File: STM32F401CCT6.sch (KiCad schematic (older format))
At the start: 37 parts, among them J1 USB_OTG, J2 Conn_02x03_Odd_Even, J3 Conn_01x20_des, J4 Conn_01x05_desc, J5 Conn_01x20, SW1 SW_Push, U1 MIC5219-3.3, U2 STM32F401CCT6, U3 USBLC6-2SC6, Y1 32.786K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

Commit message: routing
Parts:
- J1: footprint Connectors_USB:USB_Micro-B_Molex_47346-0001 -> Connectors_USB:USB_Micro-B_Molex-105017-0001
- J2: footprint Pin_Headers:Pin_Header_Straight_2x03_Pitch2.54mm_SMD -> Pin_Headers:Pin_Header_Straight_2x03_Pitch2.54mm
- Y2: footprint Crystals:Crystal_HC49-U_Vertical -> Crystals:Crystal_HC49-4H_Vertical
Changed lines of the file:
@@
 F 0 "J2" H 2750 1400 50  0000 C CNN
 F 1 "Conn_02x03_Odd_Even" H 2750 1000 50  0000 C CNN
-F 2 "Pin_Headers:Pin_Header_Straight_2x03_Pitch2.54mm_SMD" H 2700 1200 50  0001 C CNN
+F 2 "Pin_Headers:Pin_Header_Straight_2x03_Pitch2.54mm" H 2700 1200 50  0001 C CNN
 F 3 "" H 2700 1200 50  0001 C CNN
 	1    2700 1200
@@
 F 0 "J1" H 700 6750 50  0000 L CNN
 F 1 "USB_OTG" H 700 6650 50  0000 L CNN
-F 2 "Connectors_USB:USB_Micro-B_Molex_47346-0001" H 1050 6250 50  0001 C CNN
+F 2 "Connectors_USB:USB_Micro-B_Molex-105017-0001" H 1050 6250 50  0001 C CNN
 F 3 "" H 1050 6250 50  0001 C CNN
 	1    900  6300
@@
 F 0 "Y2" V 4750 6900 50  0000 C CNN
 F 1 "8MHz" V 4650 6950 50  0000 C CNN
-F 2 "Crystals:Crystal_HC49-U_Vertical" H 4750 6750 50  0001 C CNN
+F 2 "Crystals:Crystal_HC49-4H_Vertical" H 4750 6750 50  0001 C CNN
 F 3 "" H 4750 6750 50  0001 C CNN
 	1    4750 6750

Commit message: Added copper pour
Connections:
- net VCC3v3 is gone; now on net VCC: J3.18 (Pin_18), J5.1 (Pin_1), U2.24 (VDD_2), U2.36 (VDD_2), U2.48 (VDD_3), U2.9 (VDDA/VREF+)
- net +5V: now also C14.1, J4.5 (Pin_5)
- net GND: no longer C14.1, J4.4 (Pin_4)
- net RESET: now also J4.4 (Pin_4); no longer J4.5 (Pin_5)
- net D-: now reaches J1.2 (D-), R3.2
- net D+: now reaches J1.3 (D+), R4.2
- net ID: now reaches J1.4 (ID), R9.2

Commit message: rerouting (left reset)
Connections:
- net +5V: no longer C14.1, J4.5 (Pin_5)
- net GND: no longer R6.1
- net PC13: now also R6.1
- net VCC: now also C14.1, J4.5 (Pin_5)
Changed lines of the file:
@@
 $EndComp
 Text Label 6300 1550 2    60   ~ 0
-GND
+PC13
 $Comp
 L Conn_02x03_Odd_Even J2
@@
 $EndComp
 Text Label 8500 1450 2    60   ~ 0
-STM_LINK
+VCC
 $Comp
 L Conn_01x20_des J3

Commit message: Finish routing
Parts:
- D1, D2: footprint LEDs:LED_0603_HandSoldering -> LEDs:LED_0805_HandSoldering
- U2: footprint UFQFPN48:UFQFPN48 -> QFPN48:UFQFPN48
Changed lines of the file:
@@
 F 0 "U2" H 7250 4450 60  0000 C CNN
 F 1 "STM32F401CCT6" H 7300 4350 50  0000 C CNN
-F 2 "UFQFPN48:UFQFPN48" H 5700 3850 60  0001 C CNN
+F 2 "QFPN48:UFQFPN48" H 5700 3850 60  0001 C CNN
 F 3 "" H 5700 3850 60  0001 C CNN
 	1    5700 3850
@@
 F 0 "D1" H 5250 1150 50  0000 C CNN
 F 1 "LED_ALT" H 5250 950 50  0000 C CNN
-F 2 "LEDs:LED_0603_HandSoldering" H 5250 1050 50  0001 C CNN
+F 2 "LEDs:LED_0805_HandSoldering" H 5250 1050 50  0001 C CNN
 F 3 "" H 5250 1050 50  0001 C CNN
 	1    5250 1050
@@
 F 0 "D2" H 5250 1650 50  0000 C CNN
 F 1 "LED_ALT" H 5250 1450 50  0000 C CNN
-F 2 "LEDs:LED_0603_HandSoldering" H 5250 1550 50  0001 C CNN
+F 2 "LEDs:LED_0805_HandSoldering" H 5250 1550 50  0001 C CNN
 F 3 "" H 5250 1550 50  0001 C CNN
 	1    5250 1550

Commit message: Moved the pin connector to bottom layer
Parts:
- C1, C10, C11, C12, C13, C14, C2, C3, C4, C5, C6, C7, C8, C9: footprint Capacitors_SMD:C_0603_HandSoldering -> Capacitors_SMD:C_0603
- D1, D2: footprint LEDs:LED_0805_HandSoldering -> LEDs:LED_0805
- R1, R10, R2, R3, R4, R5, R6, R7, R8, R9: footprint Resistors_SMD:R_0603_HandSoldering -> Resistors_SMD:R_0603
- U1: footprint TO_SOT_Packages_SMD:SOT-23-5_HandSoldering -> TO_SOT_Packages_SMD:SOT-23-5
- U3: footprint TO_SOT_Packages_SMD:SOT-23-6_Handsoldering -> TO_SOT_Packages_SMD:SOT-23-6
- Y1: footprint Crystals:Crystal_SMD_SeikoEpson_MC306-4pin_8.0x3.2mm_HandSoldering -> Crystals:Crystal_SMD_SeikoEpson_MC306-4pin_8.0x3.2mm
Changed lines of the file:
@@
 F 0 "R5" V 6030 1050 50  0000 C CNN
 F 1 "510R,0603" V 5850 1050 50  0000 C CNN
-F 2 "Resistors_SMD:R_0603_HandSoldering" V 5880 1050 50  0001 C CNN
+F 2 "Resistors_SMD:R_0603" V 5880 1050 50  0001 C CNN
 F 3 "" H 5950 1050 50  0001 C CNN
 	1    5950 1050
@@
 F 0 "R6" V 6030 1550 50  0000 C CNN
 F 1 "510R,603" V 5850 1550 50  0000 C CNN
-F 2 "Resistors_SMD:R_0603_HandSoldering" V 5880 1550 50  0001 C CNN
+F 2 "Resistors_SMD:R_0603" V 5880 1550 50  0001 C CNN
 F 3 "" H 5950 1550 50  0001 C CNN
 	1    5950 1550
@@
 F 0 "R8" V 3330 1200 50  0000 C CNN
 F 1 "100K,0603" V 3100 1200 50  0000 C CNN
-F 2 "Resistors_SMD:R_0603_HandSoldering" V 3180 1200 50  0001 C CNN
+F 2 "Resistors_SMD:R_0603" V 3180 1200 50  0001 C CNN
 F 3 "" H 3250 1200 50  0001 C CNN
 	1    3250 1200
@@
 F 0 "R7" V 2230 1200 50  0000 C CNN
 F 1 "100K,0603" V 2000 1200 50  0000 C CNN
-F 2 "Resistors_SMD:R_0603_HandSoldering" V 2080 1200 50  0001 C CNN
+F 2 "Resistors_SMD:R_0603" V 2080 1200 50  0001 C CNN
 F 3 "" H 2150 1200 50  0001 C CNN
 	1    2150 1200
@@
 F 0 "R1" V 1130 1200 50  0000 C CNN
 F 1 "10K" V 1050 1200 50  0000 C CNN
-F 2 "Resistors_SMD:R_0603_HandSoldering" V 980 1200 50  0001 C CNN
+F 2 "Resistors_SMD:R_0603" V 980 1200 50  0001 C CNN
 F 3 "" H 1050 1200 50  0001 C CNN
 	1    1050 1200
@@
 F 0 "C3" H 1075 1700 50  0000 L CNN
 F 1 "105,0603" H 1075 1500 50  0000 L CNN
-F 2 "Capacitors_SMD:C_0603_HandSoldering" H 1088 1450 50  0001 C CNN
+F 2 "Capacitors_SMD:C_0603" H 1088 1450 50  0001 C CNN
 F 3 "" H 1050 1600 50  0001 C CNN
 	1    1050 1600
@@
 F 0 "R3" V 1800 6300 50  0000 C CNN
 F 1 "20R,0603" V 1700 6350 50  0000 C CNN
-F 2 "Resistors_SMD:R_0603_HandSoldering" V 1730 6300 50  0001 C CNN
+F 2 "Resistors_SMD:R_0603" V 1730 6300 50  0001 C CNN
 F 3 "" H 1800 6300 50  0001 C CNN
 	1    1800 6300
@@
 F 0 "R4" V 1800 6400 50  0000 C CNN
 F 1 "20R,0603" V 1900 6450 50  0000 C CNN
-F 2 "Resistors_SMD:R_0603_HandSoldering" V 1730 6400 50  0001 C CNN
+F 2 "Resistors_SMD:R_0603" V 1730 6400 50  0001 C CNN
 F 3 "" H 1800 6400 50  0001 C CNN
 	1    1800 6400
@@
 F 0 "R10" V 2150 6650 50  0000 C CNN
 F 1 "4.7K" V 2250 6650 50  0000 C CNN
-F 2 "Resistors_SMD:R_0603_HandSoldering" V 2080 6650 50  0001 C CNN
+F 2 "Resistors_SMD:R_0603" V 2080 6650 50  0001 C CNN
 F 3 "" H 2150 6650 50  0001 C CNN
 	1    2150 6650
@@
 F 0 "C6" V 4100 5550 50  0000 L CNN
 F 1 "20p,0603" V 4000 5550 50  0000 L CNN
-F 2 "Capacitors_SMD:C_0603_HandSoldering" H 4188 5550 50  0001 C CNN
+F 2 "Capacitors_SMD:C_0603" H 4188 5550 50  0001 C CNN
 F 3 "" H 4150 5700 50  0001 C CNN
 	1    4150 5700
@@
 F 0 "C7" V 4100 6050 50  0000 L CNN
 F 1 "20p,0603" V 4000 6000 50  0000 L CNN
-F 2 "Capacitors_SMD:C_0603_HandSoldering" H 4188 6050 50  0001 C CNN
+F 2 "Capacitors_SMD:C_0603" H 4188 6050 50  0001 C CNN
 F 3 "" H 4150 6200 50  0001 C CNN
 	1    4150 6200
@@
 F 0 "C10" H 4575 5200 50  0000 L CNN
 F 1 "104,0603" H 4575 5000 50  0000 L CNN
-F 2 "Capacitors_SMD:C_0603_HandSoldering" H 4588 4950 50  0001 C CNN
+F 2 "Capacitors_SMD:C_0603" H 4588 4950 50  0001 C CNN
 F 3 "" H 4550 5100 50  0001 C CNN
 	1    4550 5100
@@
 F 0 "C11" H 4975 5200 50  0000 L CNN
 F 1 "104,0603" H 4975 5000 50  0000 L CNN
-F 2 "Capacitors_SMD:C_0603_HandSoldering" H 4988 4950 50  0001 C CNN
+F 2 "Capacitors_SMD:C_0603" H 4988 4950 50  0001 C CNN
 F 3 "" H 4950 5100 50  0001 C CNN
 	1    4950 5100
@@
 F 0 "C14" H 8725 1300 50  0000 L CNN
 F 1 "104,0603" H 8725 1100 50  0000 L CNN
-F 2 "Capacitors_SMD:C_0603_HandSoldering" H 8738 1050 50  0001 C CNN
+F 2 "Capacitors_SMD:C_0603" H 8738 1050 50  0001 C CNN
 F 3 "" H 8700 1200 50  0001 C CNN
 	1    8700 1200
@@
 F 0 "Y1" V 4450 6150 50  0000 C CNN
 F 1 "32.786K" V 4350 6200 50  0000 C CNN
-F 2 "Crystals:Crystal_SMD_SeikoEpson_MC306-4pin_8.0x3.2mm_HandSoldering" H 4450 5950 50  0001 C CNN
+F 2 "Crystals:Crystal_SMD_SeikoEpson_MC306-4pin_8.0x3.2mm" H 4450 5950 50  0001 C CNN
 F 3 "" H 4450 5950 50  0001 C CNN
 	1    4450 5950
@@
 F 0 "C8" V 4300 6500 50  0000 L CNN
 F 1 "20p,0603" V 4550 6300 50  0000 L CNN
-F 2 "Capacitors_SMD:C_0603_HandSoldering" H 4438 6300 50  0001 C CNN
+F 2 "Capacitors_SMD:C_0603" H 4438 6300 50  0001 C CNN
 F 3 "" H 4400 6450 50  0001 C CNN
 	1    4400 6450
@@
 F 0 "C9" V 4550 6950 50  0000 L CNN
 F 1 "20p,0603" V 4250 6900 50  0000 L CNN
-F 2 "Capacitors_SMD:C_0603_HandSoldering" H 4438 6900 50  0001 C CNN
+F 2 "Capacitors_SMD:C_0603" H 4438 6900 50  0001 C CNN
 F 3 "" H 4400 7050 50  0001 C CNN
 	1    4400 7050
@@
 F 0 "R2" V 5300 6800 50  0000 C CNN
 F 1 "1M" V 5200 6800 50  0000 C CNN
-F 2 "Resistors_SMD:R_0603_HandSoldering" V 5130 6800 50  0001 C CNN
+F 2 "Resistors_SMD:R_0603" V 5130 6800 50  0001 C CNN
 F 3 "" H 5200 6800 50  0001 C CNN
 	1    5200 6800
@@
 F 0 "C12" H 7025 2550 50  0000 L CNN
 F 1 "104,0603" H 7025 2350 50  0000 L CNN
-F 2 "Capacitors_SMD:C_0603_HandSoldering" H 7038 2300 50  0001 C CNN
+F 2 "Capacitors_SMD:C_0603" H 7038 2300 50  0001 C CNN
 F 3 "" H 7000 2450 50  0001 C CNN
 	1    7000 2450
@@
 F 0 "C13" H 7475 2550 50  0000 L CNN
 F 1 "104,0603" H 7475 2350 50  0000 L CNN
-F 2 "Capacitors_SMD:C_0603_HandSoldering" H 7488 2300 50  0001 C CNN
+F 2 "Capacitors_SMD:C_0603" H 7488 2300 50  0001 C CNN
 F 3 "" H 7450 2450 50  0001 C CNN
 	1    7450 2450
@@
 F 0 "R9" V 1450 6500 50  0000 C CNN
 F 1 "20R,0603" V 1550 6500 50  0000 C CNN
-F 2 "Resistors_SMD:R_0603_HandSoldering" V 1380 6500 50  0001 C CNN
+F 2 "Resistors_SMD:R_0603" V 1380 6500 50  0001 C CNN
 F 3 "" H 1450 6500 50  0001 C CNN
 	1    1450 6500
@@
 F 0 "U1" H 1750 4175 50  0000 C CNN
 F 1 "MIC5219-3.3" H 1900 4175 50  0000 L CNN
-F 2 "TO_SOT_Packages_SMD:SOT-23-5_HandSoldering" H 1900 4275 50  0001 C CNN
+F 2 "TO_SOT_Packages_SMD:SOT-23-5" H 1900 4275 50  0001 C CNN
 F 3 "" H 1900 3950 50  0001 C CNN
 	1    1900 3950
@@
 F 0 "C1" H 775 4200 50  0000 L CNN
 F 1 "223,0603" H 550 4000 50  0000 L CNN
-F 2 "Capacitors_SMD:C_0603_HandSoldering" H 788 3950 50  0001 C CNN
+F 2 "Capacitors_SMD:C_0603" H 788 3950 50  0001 C CNN
 F 3 "" H 750 4100 50  0001 C CNN
 	1    750  4100
@@
 F 0 "C2" H 1025 4200 50  0000 L CNN
 F 1 "223,0603" H 1000 4000 50  0000 L CNN
-F 2 "Capacitors_SMD:C_0603_HandSoldering" H 1038 3950 50  0001 C CNN
+F 2 "Capacitors_SMD:C_0603" H 1038 3950 50  0001 C CNN
 F 3 "" H 1000 4100 50  0001 C CNN
 	1    1000 4100
@@
 F 0 "C4" H 2625 4200 50  0000 L CNN
 F 1 "106,0603" H 2350 4000 50  0000 L CNN
-F 2 "Capacitors_SMD:C_0603_HandSoldering" H 2638 3950 50  0001 C CNN
+F 2 "Capacitors_SMD:C_0603" H 2638 3950 50  0001 C CNN
 F 3 "" H 2600 4100 50  0001 C CNN
 	1    2600 4100
@@
 F 0 "C5" H 2975 4200 50  0000 L CNN
 F 1 "104,0603" H 2900 4000 50  0000 L CNN
-F 2 "Capacitors_SMD:C_0603_HandSoldering" H 2988 3950 50  0001 C CNN
+F 2 "Capacitors_SMD:C_0603" H 2988 3950 50  0001 C CNN
 F 3 "" H 2950 4100 50  0001 C CNN
 	1    2950 4100
@@
 F 0 "U3" H 2850 6350 60  0000 C CNN
 F 1 "USBLC6-2SC6" H 2900 6850 60  0000 C CNN
-F 2 "TO_SOT_Packages_SMD:SOT-23-6_Handsoldering" H 2950 6500 60  0001 C CNN
+F 2 "TO_SOT_Packages_SMD:SOT-23-6" H 2950 6500 60  0001 C CNN
 F 3 "" H 2950 6500 60  0001 C CNN
 	1    2950 6500
@@
 F 0 "D1" H 5250 1150 50  0000 C CNN
 F 1 "LED_ALT" H 5250 950 50  0000 C CNN
-F 2 "LEDs:LED_0805_HandSoldering" H 5250 1050 50  0001 C CNN
+F 2 "LEDs:LED_0805" H 5250 1050 50  0001 C CNN
 F 3 "" H 5250 1050 50  0001 C CNN
 	1    5250 1050
@@
 F 0 "D2" H 5250 1650 50  0000 C CNN
 F 1 "LED_ALT" H 5250 1450 50  0000 C CNN
-F 2 "LEDs:LED_0805_HandSoldering" H 5250 1550 50  0001 C CNN
+F 2 "LEDs:LED_0805" H 5250 1550 50  0001 C CNN
 F 3 "" H 5250 1550 50  0001 C CNN
 	1    5250 1550

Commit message: Moved the bottom edge cut further inwards
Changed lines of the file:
@@
 GND
 Text Label 8300 2950 0    60   ~ 0
-STM_LINK
+ST_LINK
 Text Label 8300 3050 0    60   ~ 0
 PB9
@@
 GND
 Text Label 1700 5900 0    60   ~ 0
-STM_LINK
+ST_LINK
 $Comp
 L LED_ALT D1

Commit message: Updated the via diamter and drill size 0.435/0.3 mm
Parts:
- added C15: 4.7u,0603, Capacitors_SMD:C_0603, symbol C
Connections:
- net GND: now also C15.1
- net PB11 renamed PB11/VCAP1
- net PB11/VCAP1: now also C15.2

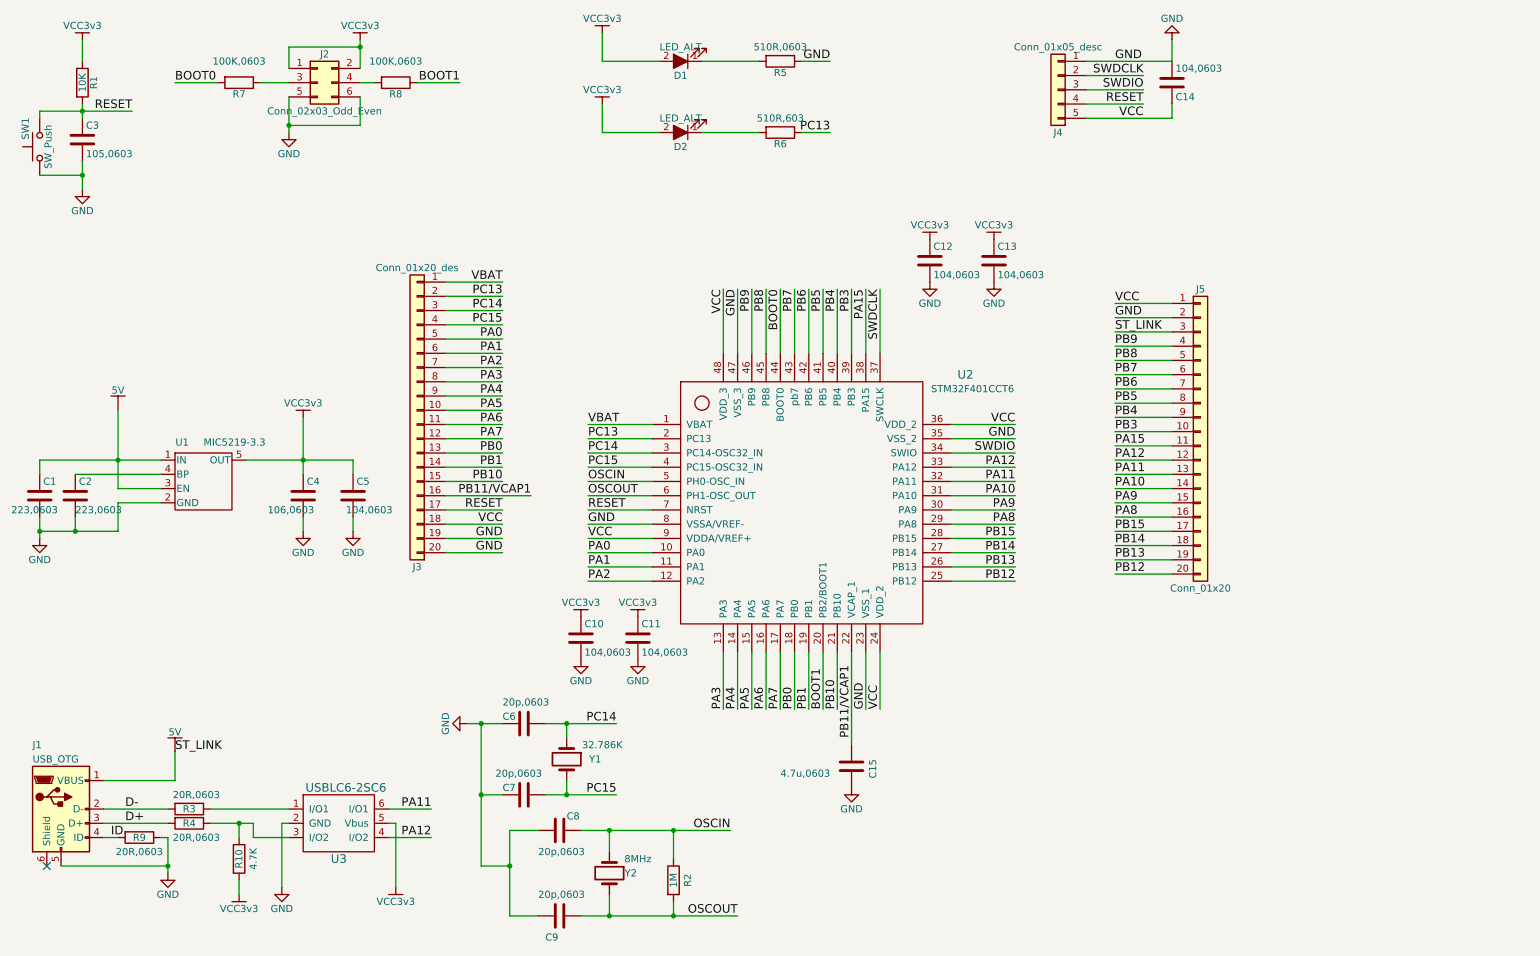
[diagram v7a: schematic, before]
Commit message: Added extra capacitor between VDD and GND (VFFA-VSSA)
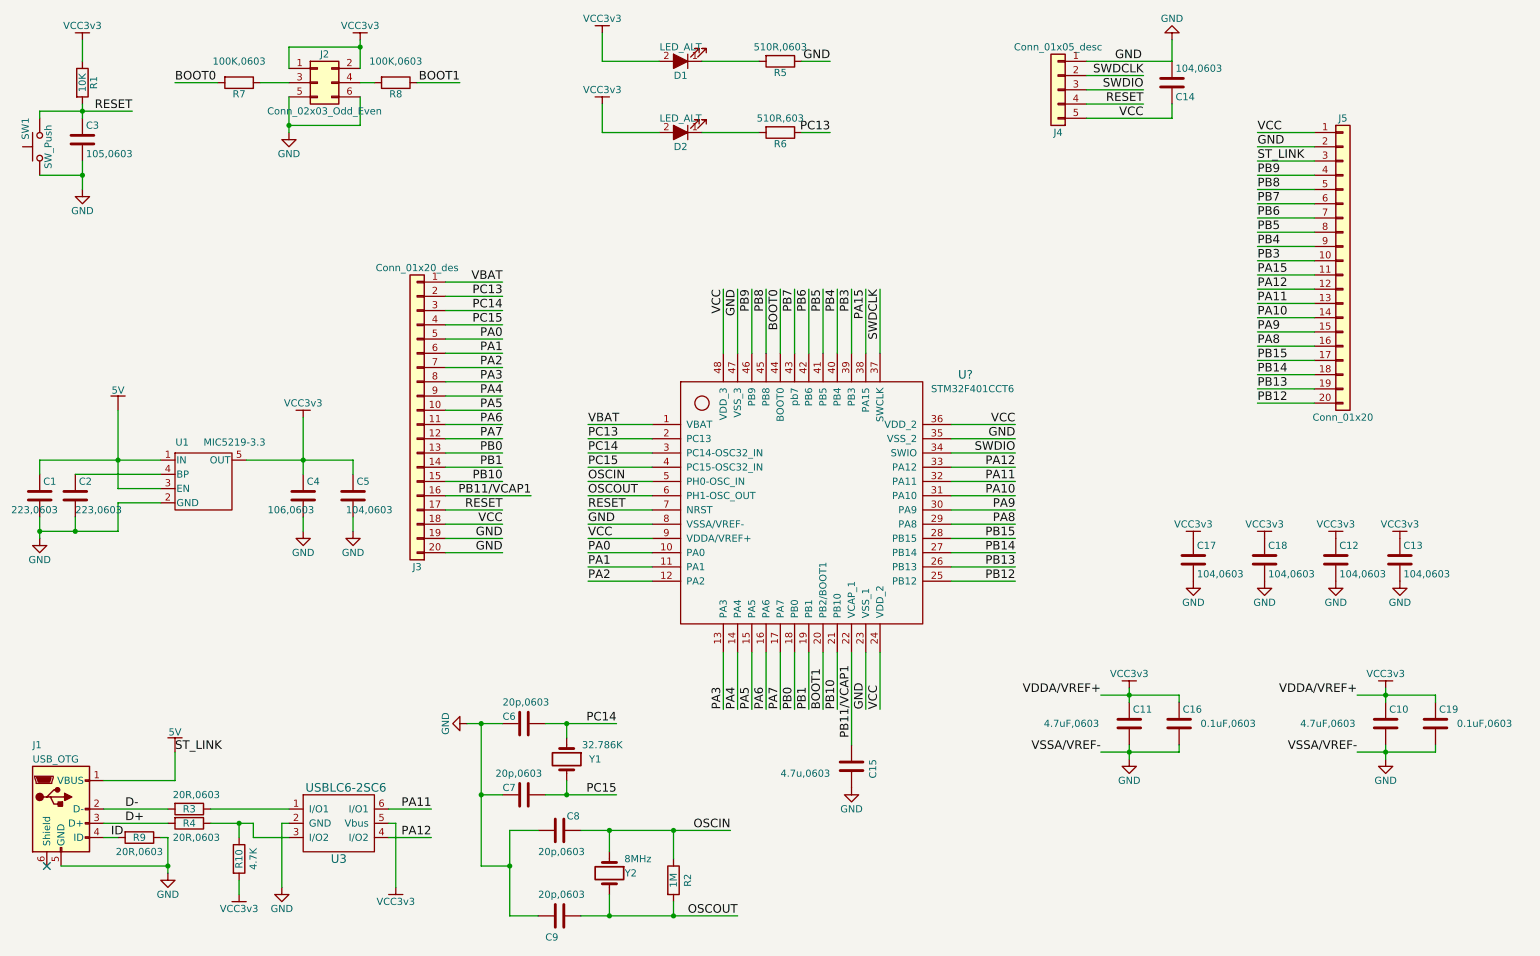
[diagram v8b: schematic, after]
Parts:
- removed U2: STM32F401CCT6, QFPN48:UFQFPN48, symbol STM32F401CCT6
- added C16, C19: 0.1uF,0603, Capacitors_SMD:C_0603, symbol C
- added C17, C18: 104,0603, Capacitors_SMD:C_0603, symbol C
- added U?: STM32F401CCT6, symbol STM32F401CCT6
- C10, C11: value 104,0603 -> 4.7uF,0603
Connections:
- net BOOT0: now also U?.44 (BOOT0)
- net BOOT1: now also U?.20 (PB2/BOOT1)
- net GND: now also C16.2, C17.2, C18.2, C19.2, U?.23 (VSS_1), U?.35 (VSS_2), U?.47 (VSS_3), U?.8 (VSSA/VREF-)
- net OSCIN: now also U?.5 (PH0-OSC_IN)
- net OSCOUT: now also U?.6 (PH1-OSC_OUT)
- net PA0: now also U?.10 (PA0)
- net PA1: now also U?.11 (PA1)
- net PA10: now also U?.31 (PA10)
- net PA11: now also U?.32 (PA11)
- net PA12: now also U?.33 (PA12)
- net PA15: now also U?.38 (PA15)
- net PA2: now also U?.12 (PA2)
- net PA3: now also U?.13 (PA3)
- net PA4: now also U?.14 (PA4)
- net PA5: now also U?.15 (PA5)
- net PA6: now also U?.16 (PA6)
- net PA7: now also U?.17 (PA7)
- net PA8: now also U?.29 (PA8)
- net PA9: now also U?.30 (PA9)
- net PB0: now also U?.18 (PB0)
- net PB1: now also U?.19 (PB1)
- net PB10: now also U?.21 (PB10)
- net PB11/VCAP1: now also U?.22 (VCAP_1)
- net PB12: now also U?.25 (PB12)
- net PB13: now also U?.26 (PB13)
- net PB14: now also U?.27 (PB14)
- net PB15: now also U?.28 (PB15)
- net PB3: now also U?.39 (PB3)
- net PB4: now also U?.40 (PB4)
- net PB5: now also U?.41 (PB5)
- net PB6: now also U?.42 (PB6)
- net PB7: now also U?.43 (pb7)
- net PB8: now also U?.45 (PB8)
- net PB9: now also U?.46 (PB9)
- net PC13: now also U?.2 (PC13)
- net PC14: now also U?.3 (PC14-OSC32_IN)
- net PC15: now also U?.4 (PC15-OSC32_IN)
- net RESET: now also U?.7 (NRST)
- net SWDCLK: now also U?.37 (SWCLK)
- net SWDIO: now also U?.34 (SWIO)
- net VBAT: now also U?.1 (VBAT)
- net VCC: now also C16.1, C17.1, C18.1, C19.1, U?.24 (VDD_2), U?.36 (VDD_2), U?.48 (VDD_3), U?.9 (VDDA/VREF+)
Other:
- moved on the sheet: C10, C12, C13, J5
